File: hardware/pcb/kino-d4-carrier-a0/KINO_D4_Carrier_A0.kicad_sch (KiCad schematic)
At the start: 0 parts

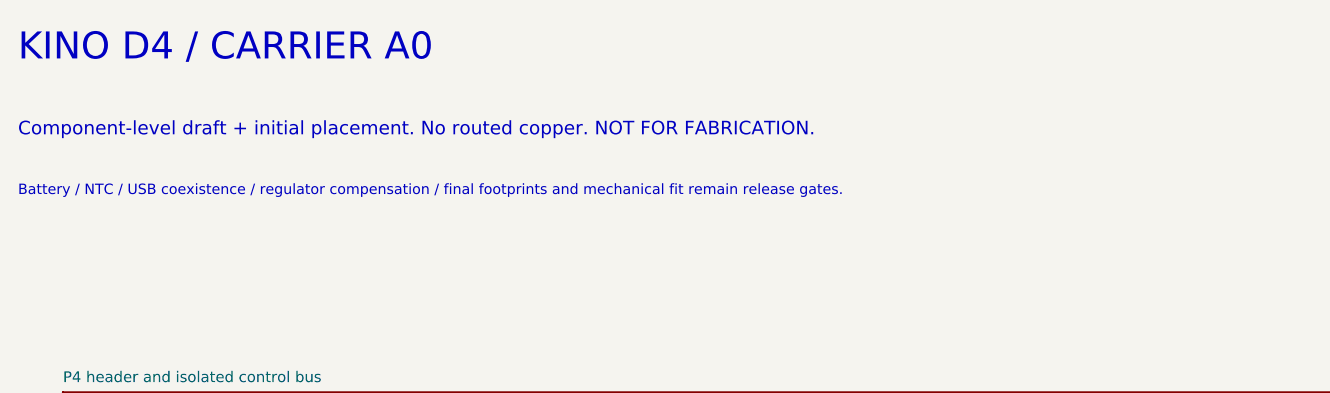
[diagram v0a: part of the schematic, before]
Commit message: feat(hardware): carrier A0.2 release pass - ready for fabrication with manual checks
Release review of the routed A0.2 carrier (A02-RELEASE.md: release matrix,
manual checks before ordering, bring-up tests). Final status: READY FOR
FABRICATION WITH SPECIFIC MANUAL CHECKS.

- USB-C input survives an unprogrammed STUSB4500 (20 V): D1001 SMF22A,
  R1004 10k, PD and load-switch P-FETs AO4409.
- Boost enable: R1204 100k BOOST_ENABLE to SYS_RAW (LTC2955-1 EN is a 2 uA
  source), Q1202 PMV16UN.
- I2C buffer U100 sides swapped (local bus on the TCA9517 A side's hard
  low); R100/R101 2.2k/22k hold EN low with JP1 pin 1 open.
- R105 SYNC_MASTER pull-down; D903 ESD on FN_N; TP1001 removed.
- SYS_RAW battery path as B.Cu and In2 pours with 25 extra vias; 1 oz inner
  copper in the stackup.
- XIAO socket pads get their solder-mask openings (footprint generator bug).
- Three fiducials per face; vias out of and away from pads; U1200 outline and
  pin-1 mark; legend lines and strokes 0.15 mm; silk association pass;
  CARRIER A0.2 / 2026-10 / S/N marking.
- Fab package (fab_a02.py): Gerbers + job file, drill, zip, placement files,
  fab BOM matched to LCSC by part number, hand-fit socket list, fab notes.
- Firmware constants header kino_carrier_a02.h.

DRC 0 / unconnected 0, ERC 0, verify.py --a02 passes.

Co-Authored-By: Claude Opus 5.5 <noreply@anthropic.com>
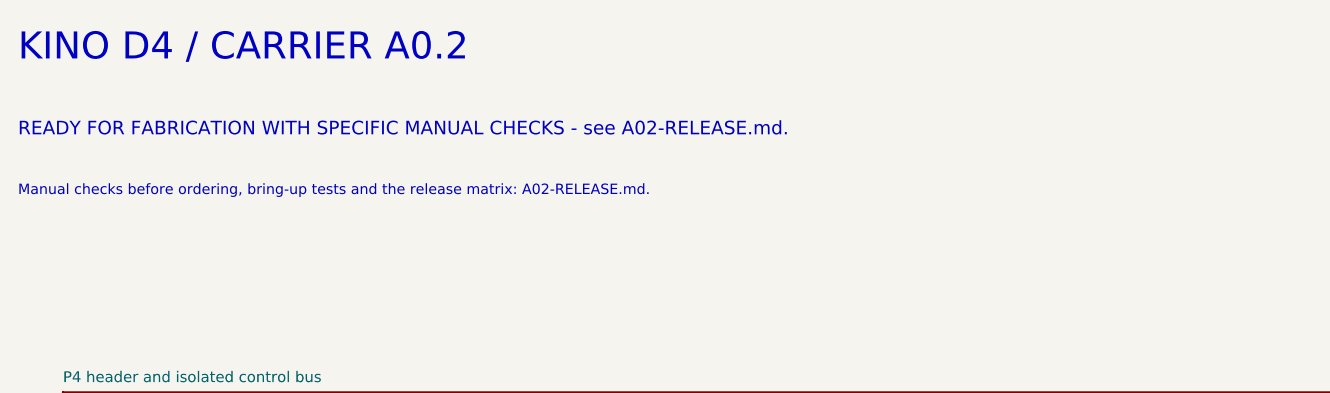
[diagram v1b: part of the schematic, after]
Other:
- note added: "KINO D4 / CARRIER A0.2"
- note added: "Manual checks before ordering, bring-up tests and the release matrix: A02-RELEASE.md."
- note added: "READY FOR FABRICATION WITH SPECIFIC MANUAL CHECKS - see A02-RELEASE.md."
- note removed: "Battery / NTC / USB coexistence / regulator compensation / final footprints and mechanical fit remain release gates."
- note removed: "Component-level draft + initial placement. No routed copper. NOT FOR FABRICATION."
- note removed: "KINO D4 / CARRIER A0"
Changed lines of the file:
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@@
     (title_block (title "KINO D4 - four-XIAO carrier A0") (date "2026-09-30") (rev "A0-DRAFT")
       (company "KINO") (comment 1 "ENGINEERING DRAFT - NOT FOR FABRICATION"))
-(text "KINO D4 / CARRIER A0" (at 20 15 0) (effects (font (size 3 3)) (justify left top)))
-(text "Component-level draft + initial placement. No routed copper. NOT FOR FABRICATION." (at 20 25 0) (effects (font (size 1.5 1.5)) (justify left top)))
-(text "Battery / NTC / USB coexistence / regulator compensation / final footprints and mechanical fit remain release gates." (at 20 32 0) (effects (font (size 1.15 1.15)) (justify left top)))
+(text "KINO D4 / CARRIER A0.2" (at 20 15 0) (effects (font (size 3 3)) (justify left top)))
+(text "READY FOR FABRICATION WITH SPECIFIC MANUAL CHECKS - see A02-RELEASE.md." (at 20 25 0) (effects (font (size 1.5 1.5)) (justify left top)))
+(text "Manual checks before ordering, bring-up tests and the release matrix: A02-RELEASE.md." (at 20 32 0) (effects (font (size 1.15 1.15)) (justify left top)))
 (sheet (at 25 55) (size 158 34) (exclude_from_sim no) (in_bom yes) (on_board yes) (dnp no)
         (stroke (width 0.25) (type solid)) (fill (color 0 0 0 0))
